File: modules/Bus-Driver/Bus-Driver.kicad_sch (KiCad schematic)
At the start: 23 parts, among them J1 WQP-PJ398, J2 WQP-PJ398, J3 WQP-PJ398, J4 WQP-PJ398, J5 Conn_01x08, J6 Conn_Front, J7 Conn_Front, J8 Conn_Back, J9 Conn_Back, SW1 SW_DPDT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

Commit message: Bus-Driver - wip
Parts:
- C1, C2: Distributor2 (none) -> Thonk; DistributorPartLink https://www.mouser.ca/ProductDetail/Panasonic/EEA-FC1E100?q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 -> https://www.mouser.ca/ProductDetail/667-ECE-A1VKS100I; DistributorPartLink2 (none) -> https://www.thonk.co.uk/shop/eurorack-diy-essentials/; DistributorPartNum 667-EEA-FC1E100 -> 667-ECE-A1VKS100I; DistributorPartNum2 (none) -> Group_Eurorack_DIY_Essential; ManufacturerPartNum EEA-FC1E100 -> ECE-A1VKS100I; Note (none) -> 12 V decoupling; Value2 25 VDC -> 35 VDC
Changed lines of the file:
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@@
     (pin "TN")
   )
-  (symbol (lib_id "-lmp-synth:CP_10U") (at 134.62 118.11 0) (unit 1)
+  (symbol (lib_name "CP_10U_1") (lib_id "-lmp-synth:CP_10U") (at 134.62 118.11 0) (unit 1)
     (in_bom yes) (on_board yes)
     (property "Reference" "C2" (id 0) (at 137.6172 116.9416 0)
@@
       (effects (font (size 1.27 1.27)) hide)
     )
-    (property "Datasheet" "https://industrial.panasonic.com/cdbs/www-data/pdf/RDF0000/ABA0000C1209.pdf" (id 3) (at 134.62 118.11 0)
+    (property "Datasheet" "https://www.mouser.ca/datasheet/2/315/ABA0000C1059-947582.pdf" (id 3) (at 134.62 118.11 0)
       (effects (font (size 1.27 1.27)) hide)
     )
@@
       (effects (font (size 1.27 1.27)) hide)
     )
-    (property "ManufacturerPartNum" "EEA-FC1E100" (id 5) (at 134.62 118.11 0)
+    (property "ManufacturerPartNum" "ECE-A1VKS100I" (id 5) (at 134.62 118.11 0)
       (effects (font (size 1.27 1.27)) hide)
     )
@@
       (effects (font (size 1.27 1.27)) hide)
     )
-    (property "DistributorPartNum" "667-EEA-FC1E100" (id 7) (at 134.62 118.11 0)
-      (effects (font (size 1.27 1.27)) hide)
-    )
-    (property "DistributorPartLink" "https://www.mouser.ca/ProductDetail/Panasonic/EEA-FC1E100?qs=nLJruSqDb94EJwiFQJd4iw%3D%3D" (id 8) (at 134.62 118.11 0)
+    (property "DistributorPartNum" "667-ECE-A1VKS100I" (id 7) (at 134.62 118.11 0)
+      (effects (font (size 1.27 1.27)) hide)
+    )
+    (property "DistributorPartLink" "https://www.mouser.ca/ProductDetail/667-ECE-A1VKS100I" (id 8) (at 134.62 118.11 0)
       (effects (font (size 1.27 1.27)) hide)
     )
@@
       (effects (font (size 1.27 1.27)) hide)
     )
-    (property "Value2" "25 VDC" (id 10) (at 134.62 118.11 0)
+    (property "Value2" "35 VDC" (id 10) (at 134.62 118.11 0)
+      (effects (font (size 1.27 1.27)) hide)
+    )
+    (property "Note" "12 V decoupling" (id 11) (at 135.255 124.46 0)
+      (effects (font (size 1.27 1.27)) (justify left) hide)
+    )
+    (property "Distributor2" "Thonk" (id 12) (at 134.62 121.92 0)
+      (effects (font (size 1.27 1.27)) hide)
+    )
+    (property "DistributorPartNum2" "Group_Eurorack_DIY_Essential" (id 13) (at 134.62 121.92 0)
+      (effects (font (size 1.27 1.27)) hide)
+    )
+    (property "DistributorPartLink2" "https://www.thonk.co.uk/shop/eurorack-diy-essentials/" (id 14) (at 134.62 121.92 0)
       (effects (font (size 1.27 1.27)) hide)
     )
@@
       (effects (font (size 1.27 1.27)) hide)
     )
-    (property "Datasheet" "https://industrial.panasonic.com/cdbs/www-data/pdf/RDF0000/ABA0000C1209.pdf" (id 3) (at 134.62 110.49 0)
+    (property "Datasheet" "https://www.mouser.ca/datasheet/2/315/ABA0000C1059-947582.pdf" (id 3) (at 134.62 110.49 0)
       (effects (font (size 1.27 1.27)) hide)
     )
@@
       (effects (font (size 1.27 1.27)) hide)
     )
-    (property "ManufacturerPartNum" "EEA-FC1E100" (id 5) (at 134.62 110.49 0)
+    (property "ManufacturerPartNum" "ECE-A1VKS100I" (id 5) (at 134.62 110.49 0)
       (effects (font (size 1.27 1.27)) hide)
     )
@@
       (effects (font (size 1.27 1.27)) hide)
     )
-    (property "DistributorPartNum" "667-EEA-FC1E100" (id 7) (at 134.62 110.49 0)
-      (effects (font (size 1.27 1.27)) hide)
-    )
-    (property "DistributorPartLink" "https://www.mouser.ca/ProductDetail/Panasonic/EEA-FC1E100?qs=nLJruSqDb94EJwiFQJd4iw%3D%3D" (id 8) (at 134.62 110.49 0)
-      (effects (font (size 1.27 1.27)) hide)
-    )
-    (property "Value2" "25 VDC" (id 9) (at 134.62 110.49 0)
+    (property "DistributorPartNum" "667-ECE-A1VKS100I" (id 7) (at 134.62 110.49 0)
+      (effects (font (size 1.27 1.27)) hide)
+    )
+    (property "DistributorPartLink" "https://www.mouser.ca/ProductDetail/667-ECE-A1VKS100I" (id 8) (at 134.62 110.49 0)
+      (effects (font (size 1.27 1.27)) hide)
+    )
+    (property "Value2" "35 VDC" (id 9) (at 134.62 110.49 0)
       (effects (font (size 1.27 1.27)) hide)
     )
@@
       (effects (font (size 1.27 1.27)) hide)
     )
+    (property "Note" "12 V decoupling" (id 11) (at 135.255 116.84 0)
+      (effects (font (size 1.27 1.27)) (justify left) hide)
+    )
+    (property "Distributor2" "Thonk" (id 12) (at 134.62 114.3 0)
+      (effects (font (size 1.27 1.27)) hide)
+    )
+    (property "DistributorPartNum2" "Group_Eurorack_DIY_Essential" (id 13) (at 134.62 114.3 0)
+      (effects (font (size 1.27 1.27)) hide)
+    )
+    (property "DistributorPartLink2" "https://www.thonk.co.uk/shop/eurorack-diy-essentials/" (id 14) (at 134.62 114.3 0)
+      (effects (font (size 1.27 1.27)) hide)
+    )

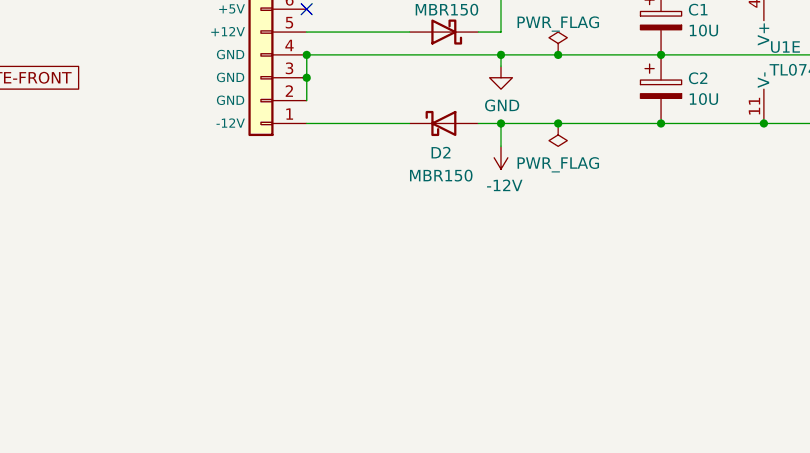
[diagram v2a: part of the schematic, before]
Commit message: Bus-Driver - add power cable
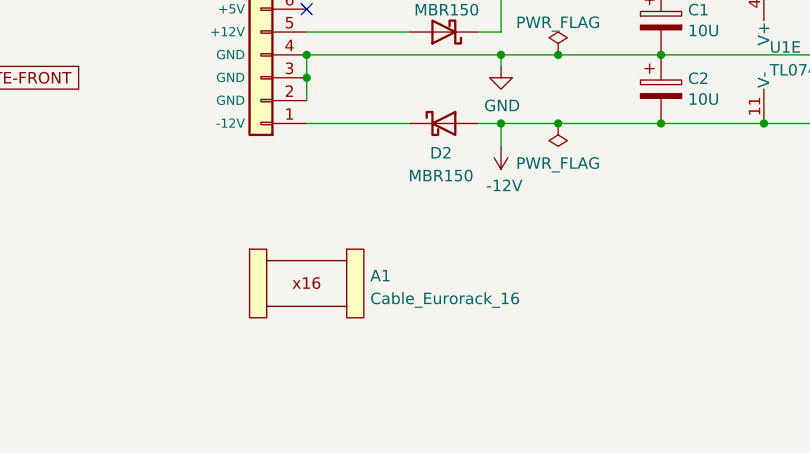
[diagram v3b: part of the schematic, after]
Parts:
- added A1: Cable_Eurorack_16, -lmp-misc:NoFootprint, symbol -lmp-synth:Cable_Eurorack_16
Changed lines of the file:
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@@
   (symbol (lib_id "-lmp-power:GND") (at 106.68 31.75 270) (unit 1)
     (in_bom yes) (on_board yes) (fields_autoplaced)
-    (property "Reference" "#PWR06" (id 0) (at 100.33 31.75 0)
+    (property "Reference" "#PWR03" (id 0) (at 100.33 31.75 0)
       (effects (font (size 1.27 1.27)) hide)
     )
@@
     )
     (pin "1")
+  )
+  (symbol (lib_id "-lmp-synth:Cable_Eurorack_16") (at 95.25 139.7 0) (unit 1)
+    (in_bom yes) (on_board no) (fields_autoplaced)
+    (property "Reference" "A1" (id 0) (at 102.3112 138.8653 0)
+      (effects (font (size 1.27 1.27)) (justify left))
+    )
+    (property "Value" "Cable_Eurorack_16" (id 1) (at 102.3112 141.4022 0)
+      (effects (font (size 1.27 1.27)) (justify left))
+    )
+    (property "Footprint" "-lmp-misc:NoFootprint" (id 2) (at 95.885 144.78 0)
+      (effects (font (size 1.27 1.27)) hide)
+    )
+    (property "Datasheet" "" (id 3) (at 95.25 131.445 0)
+      (effects (font (size 1.27 1.27)) hide)
+    )
+    (property "Note" "Length as required" (id 4) (at 95.25 140.97 0)
+      (effects (font (size 1.27 1.27)) hide)
+    )
+    (property "Distributor" "Thonk" (id 5) (at 95.25 144.78 0)
+      (effects (font (size 1.27 1.27)) hide)
+    )
+    (property "DistributorPartLink" "https://www.thonk.co.uk/shop/eurorack-power-cables/" (id 6) (at 95.25 144.78 0)
+      (effects (font (size 1.27 1.27)) hide)
+    )
+    (property "Distributor2" "SynthCube" (id 7) (at 95.25 144.78 0)
+      (effects (font (size 1.27 1.27)) hide)
+    )
+    (property "DistributorPartLink2" "https://synthcube.com/cart/eurorack-ribbon-power-cables" (id 8) (at 95.25 144.78 0)
+      (effects (font (size 1.27 1.27)) hide)
+    )
+    (property "Distributor3" "Modular Addict" (id 9) (at 95.25 144.78 0)
+      (effects (font (size 1.27 1.27)) hide)
+    )
+    (property "DistributorPartLink3" "https://modularaddict.com/parts/eurorack-power-cables-1" (id 10) (at 95.25 144.78 0)
+      (effects (font (size 1.27 1.27)) hide)
+    )
   )
   (symbol (lib_id "-lmp:R_1%_0W166") (at 191.77 88.9 0) (unit 1)
@@
   (symbol (lib_id "-lmp-power:GND") (at 106.68 68.58 270) (unit 1)
     (in_bom yes) (on_board yes) (fields_autoplaced)
-    (property "Reference" "#PWR07" (id 0) (at 100.33 68.58 0)
+    (property "Reference" "#PWR04" (id 0) (at 100.33 68.58 0)
       (effects (font (size 1.27 1.27)) hide)
     )
@@
   (symbol (lib_id "-lmp-power:+12V") (at 116.84 104.14 0) (unit 1)
     (in_bom yes) (on_board yes)
-    (property "Reference" "#PWR03" (id 0) (at 116.84 107.95 0)
+    (property "Reference" "#PWR05" (id 0) (at 116.84 107.95 0)
       (effects (font (size 1.27 1.27)) hide)
     )
@@
   (symbol (lib_id "-lmp-power:-12V") (at 116.84 124.46 0) (unit 1)
     (in_bom yes) (on_board yes)
-    (property "Reference" "#PWR05" (id 0) (at 116.84 120.65 0)
+    (property "Reference" "#PWR07" (id 0) (at 116.84 120.65 0)
       (effects (font (size 1.27 1.27)) hide)
     )
@@
   (symbol (lib_id "-lmp-power:GND") (at 116.84 115.57 0) (unit 1)
     (in_bom yes) (on_board yes)
-    (property "Reference" "#PWR04" (id 0) (at 116.84 121.92 0)
+    (property "Reference" "#PWR06" (id 0) (at 116.84 121.92 0)
       (effects (font (size 1.27 1.27)) hide)
     )
@@
       (reference "#PWR02") (unit 1) (value "GND") (footprint "")
     )
+    (path "/00e5cd6d-991a-4fd8-9bfa-00c234dec496"
+      (reference "#PWR03") (unit 1) (value "GND") (footprint "")
+    )
+    (path "/61694b61-65e9-49fc-b80c-adbad830c0df"
+      (reference "#PWR04") (unit 1) (value "GND") (footprint "")
+    )
     (path "/66a7c90d-0d12-4607-aa94-775b74835ae4"
-      (reference "#PWR03") (unit 1) (value "+12V") (footprint "")
+      (reference "#PWR05") (unit 1) (value "+12V") (footprint "")
     )
     (path "/d6b1d028-79b3-4068-a7bc-3e90dbfdd5c9"
-      (reference "#PWR04") (unit 1) (value "GND") (footprint "")
+      (reference "#PWR06") (unit 1) (value "GND") (footprint "")
     )
     (path "/b1c4f5e7-18da-41ce-9dd1-cd6e740715cd"
-      (reference "#PWR05") (unit 1) (value "-12V") (footprint "")
-    )
-    (path "/00e5cd6d-991a-4fd8-9bfa-00c234dec496"
-      (reference "#PWR06") (unit 1) (value "GND") (footprint "")
-    )
-    (path "/61694b61-65e9-49fc-b80c-adbad830c0df"
-      (reference "#PWR07") (unit 1) (value "GND") (footprint "")
+      (reference "#PWR07") (unit 1) (value "-12V") (footprint "")
     )
     (path "/90a9d4d2-6841-4e20-8e8e-781c59b0cdec"
@@
       (reference "#PWR011") (unit 1) (value "GND") (footprint "")
     )
+    (path "/0c547f9e-be9c-43dc-b85c-90ef5c85d878"
+      (reference "A1") (unit 1) (value "Cable_Eurorack_16") (footprint "-lmp-misc:NoFootprint")
+    )
     (path "/85783dae-6f80-4835-b5db-61dffd842eac"

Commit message: Bus-Driver: BOM fix
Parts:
- J8: DistributorPartLink 649-1012937993601BLF -> https://www.adafruit.com/product/1540
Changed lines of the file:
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@@
       (effects (font (size 1.27 1.27)) hide)
     )
-    (property "DistributorPartLink" "649-1012937993601BLF" (id 6) (at 125.73 36.83 0)
+    (property "DistributorPartLink" "https://www.adafruit.com/product/1540" (id 6) (at 125.73 36.83 0)
       (effects (font (size 1.27 1.27)) hide)
     )

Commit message: Bus-Driver: Remove a redundant field from some schematic items
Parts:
- C1, C2: Note  12 V decoupling -> (none)
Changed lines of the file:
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@@
-      (effects (font (size 1.27 1.27)) hide)
-    )
-    (property "Note " "12 V decoupling" (id 10) (at 134.62 110.49 0)
       (effects (font (size 1.27 1.27)) hide)
     )
@@
       (effects (font (size 1.27 1.27)) hide)
     )
-    (property "Note " "12 V decoupling" (id 10) (at 134.62 118.11 0)
-      (effects (font (size 1.27 1.27)) hide)
-    )

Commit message: Buff-Mult - Improved precision (#43)
Improved precision in the output stage
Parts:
- R3, R4, R5, R6: value 51R -> 270R; DistributorPartLink https://www.mouser.ca/ProductDetail/?qs=oAGoVhmvjhzVx2bdEH1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 -> https://www.mouser.ca/ProductDetail/603-MFR-25FRF52-270R; DistributorPartNum 603-MFR-25FBF52-51R -> 603-MFR-25FRF52-270R; ManufacturerPartNum MFR-25FBF52-51R -> MFR-25FRF52-270R
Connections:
- net OUT-CV-BUS: now also U1.13 (-)
- net OUT-CV-FRONT: now also U1.9 (-)
- net OUT-GATE-BUS: now also U1.2 (-)
- net OUT-GATE-FRONT: now also U1.6 (-)
- net at R3.1, U1.8: no longer U1.9 (-)
- net at R6.1, U1.1: no longer U1.2 (-)
- net at R5.1, U1.7: no longer U1.6 (-)
- net at R4.1, U1.14: no longer U1.13 (-)
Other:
- moved on the sheet: C1, C2, C3, C4, R3, R4, R5, R6, U1E

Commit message: Bus-Driver: Improved accuracy (#44)
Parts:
- R1, R2: DistributorPartLink https://www.mouser.ca/c/?m=YAGEO&power+rating=166+mW+(1%2f6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 -> https://www.mouser.ca/ProductDetail/YAGEO/MFR-12FTF52-1M?qs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; DistributorPartNum 603-MFR-12* -> 603-MFR-12FTF52-1M; ManufacturerPartNum MFR-12* -> MFR-12FTF52-1M
- R3, R4, R5, R6: DistributorPartLink https://www.mouser.ca/ProductDetail/603-MFR-25FRF52-270R -> https://www.mouser.ca/ProductDetail/YAGEO/MFR-25FRF52-270R?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
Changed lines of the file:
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@@
       (effects (font (size 1.27 1.27)) hide)
     )
-    (property "ManufacturerPartNum" "MFR-12*" (id 5) (at 191.77 88.9 0)
+    (property "ManufacturerPartNum" "MFR-12FTF52-1M" (id 5) (at 191.77 88.9 0)
       (effects (font (size 1.27 1.27)) hide)
     )
@@
       (effects (font (size 1.27 1.27)) hide)
     )
-    (property "DistributorPartNum" "603-MFR-12*" (id 7) (at 191.77 88.9 0)
-      (effects (font (size 1.27 1.27)) hide)
-    )
-    (property "DistributorPartLink" "https://www.mouser.ca/c/?m=YAGEO&power+rating=166+mW+(1%2f6+W)&tolerance=1+%25&instock=y" (id 8) (at 191.77 88.9 0)
+    (property "DistributorPartNum" "603-MFR-12FTF52-1M" (id 7) (at 191.77 88.9 0)
+      (effects (font (size 1.27 1.27)) hide)
+    )
+    (property "DistributorPartLink" "https://www.mouser.ca/ProductDetail/YAGEO/MFR-12FTF52-1M?qs=oAGoVhmvjhw%2F%2F4epxEjLtQ%3D%3D" (id 8) (at 191.77 88.9 0)
       (effects (font (size 1.27 1.27)) hide)
     )
@@
       (effects (font (size 1.27 1.27)) hide)
     )
-    (property "ManufacturerPartNum" "MFR-12*" (id 5) (at 191.77 38.1 0)
+    (property "ManufacturerPartNum" "MFR-12FTF52-1M" (id 5) (at 191.77 38.1 0)
       (effects (font (size 1.27 1.27)) hide)
     )
@@
       (effects (font (size 1.27 1.27)) hide)
     )
-    (property "DistributorPartNum" "603-MFR-12*" (id 7) (at 191.77 38.1 0)
-      (effects (font (size 1.27 1.27)) hide)
-    )
-    (property "DistributorPartLink" "https://www.mouser.ca/c/?m=YAGEO&power+rating=166+mW+(1%2f6+W)&tolerance=1+%25&instock=y" (id 8) (at 191.77 38.1 0)
+    (property "DistributorPartNum" "603-MFR-12FTF52-1M" (id 7) (at 191.77 38.1 0)
+      (effects (font (size 1.27 1.27)) hide)
+    )
+    (property "DistributorPartLink" "https://www.mouser.ca/ProductDetail/YAGEO/MFR-12FTF52-1M?qs=oAGoVhmvjhw%2F%2F4epxEjLtQ%3D%3D" (id 8) (at 191.77 38.1 0)
       (effects (font (size 1.27 1.27)) hide)
     )
@@
       (effects (font (size 1.27 1.27)) hide)
     )
-    (property "DistributorPartLink" "https://www.mouser.ca/ProductDetail/603-MFR-25FRF52-270R" (id 10) (at 224.79 110.49 0)
+    (property "DistributorPartLink" "https://www.mouser.ca/ProductDetail/YAGEO/MFR-25FRF52-270R?qs=oAGoVhmvjhzmtEYPI6wC%2FA%3D%3D" (id 10) (at 224.79 110.49 0)
       (effects (font (size 1.27 1.27)) hide)
     )
@@
     (pin "1")
   )
-  (symbol (lib_name "R_51R_Output_2") (lib_id "-lmp-synth:R_51R_Output") (at 224.79 59.69 90) (unit 1)
+  (symbol (lib_id "-lmp-synth:R_51R_Output") (at 224.79 59.69 90) (unit 1)
     (in_bom yes) (on_board yes) (fields_autoplaced)
     (property "Reference" "R4" (id 0) (at 224.79 52.4374 90))
@@
       (effects (font (size 1.27 1.27)) hide)
     )
-    (property "DistributorPartLink" "https://www.mouser.ca/ProductDetail/603-MFR-25FRF52-270R" (id 10) (at 224.79 59.69 0)
-      (effects (font (size 1.27 1.27)) hide)
-    )
-    (pin "1")
-    (pin "2")
-  )
-  (symbol (lib_name "R_51R_Output_1") (lib_id "-lmp-synth:R_51R_Output") (at 224.79 35.56 90) (unit 1)
+    (property "DistributorPartLink" "https://www.mouser.ca/ProductDetail/YAGEO/MFR-25FRF52-270R?qs=oAGoVhmvjhzmtEYPI6wC%2FA%3D%3D" (id 10) (at 224.79 59.69 0)
+      (effects (font (size 1.27 1.27)) hide)
+    )
+    (pin "1")
+    (pin "2")
+  )
+  (symbol (lib_id "-lmp-synth:R_51R_Output") (at 224.79 35.56 90) (unit 1)
     (in_bom yes) (on_board yes) (fields_autoplaced)
     (property "Reference" "R3" (id 0) (at 224.79 28.3074 90))
@@
       (effects (font (size 1.27 1.27)) hide)
     )
-    (property "DistributorPartLink" "https://www.mouser.ca/ProductDetail/603-MFR-25FRF52-270R" (id 10) (at 224.79 35.56 0)
-      (effects (font (size 1.27 1.27)) hide)
-    )
-    (pin "1")
-    (pin "2")
-  )
-  (symbol (lib_name "CP_10U_1") (lib_id "-lmp-synth:CP_10U") (at 127 110.49 0) (unit 1)
+    (property "DistributorPartLink" "https://www.mouser.ca/ProductDetail/YAGEO/MFR-25FRF52-270R?qs=oAGoVhmvjhzmtEYPI6wC%2FA%3D%3D" (id 10) (at 224.79 35.56 0)
+      (effects (font (size 1.27 1.27)) hide)
+    )
+    (pin "1")
+    (pin "2")
+  )
+  (symbol (lib_id "-lmp-synth:CP_10U") (at 127 110.49 0) (unit 1)
     (in_bom yes) (on_board yes)
     (property "Reference" "C1" (id 0) (at 129.9972 109.3216 0)
@@
     (pin "4")
   )
-  (symbol (lib_name "R_51R_Output_3") (lib_id "-lmp-synth:R_51R_Output") (at 224.79 86.36 90) (unit 1)
+  (symbol (lib_id "-lmp-synth:R_51R_Output") (at 224.79 86.36 90) (unit 1)
     (in_bom yes) (on_board yes) (fields_autoplaced)
     (property "Reference" "R5" (id 0) (at 224.79 79.1074 90))
@@
       (effects (font (size 1.27 1.27)) hide)
     )
-    (property "DistributorPartLink" "https://www.mouser.ca/ProductDetail/603-MFR-25FRF52-270R" (id 10) (at 224.79 86.36 0)
-      (effects (font (size 1.27 1.27)) hide)
-    )
+    (property "DistributorPartLink" "https://www.mouser.ca/ProductDetail/YAGEO/MFR-25FRF52-270R?qs=oAGoVhmvjhzmtEYPI6wC%2FA%3D%3D" (id 10) (at 224.79 86.36 0)
+      (effects (font (size 1.27 1.27)) hide)
+    )
